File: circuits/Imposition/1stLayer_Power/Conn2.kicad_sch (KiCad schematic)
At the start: 3 parts, among them J12 Conn_01x02_Male

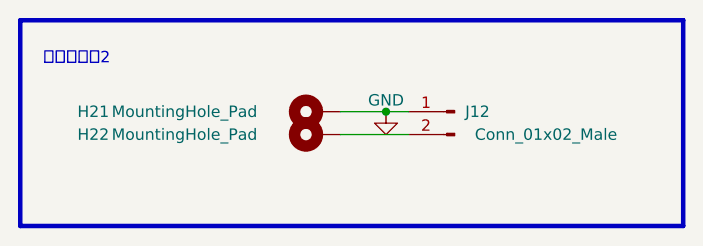
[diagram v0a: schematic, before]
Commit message: 発注_第一弾
Drive, 1stLayer_Power, 2ndLayer_3rdLayer
を発注
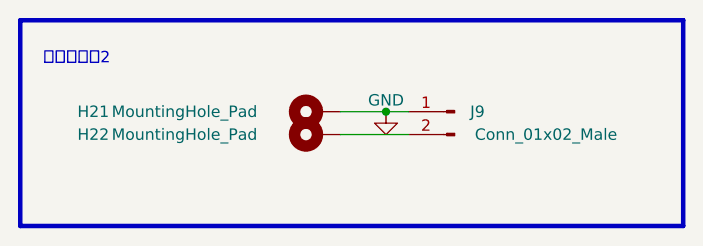
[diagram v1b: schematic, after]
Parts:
- renumbered J12 to J9
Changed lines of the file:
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@@
   (symbol (lib_id "Connector:Conn_01x02_Male") (at 160.02 106.68 0) (mirror y) (unit 1)
     (in_bom yes) (on_board yes) (dnp no)
-    (property "Reference" "J12" (at 162.56 106.68 0)
+    (property "Reference" "J9" (at 162.56 106.68 0)
       (effects (font (size 1.27 1.27)))
     )
@@
       (project "1stLayer_Power"
         (path "/599e2e4a-5379-461e-b684-22a177410a52/853e7d82-0cb0-4011-9178-97eaeea1569d"
-          (reference "J12") (unit 1)
+          (reference "J9") (unit 1)
         )
       )
